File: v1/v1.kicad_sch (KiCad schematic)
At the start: 61 parts, among them CON1 SNES-CONN

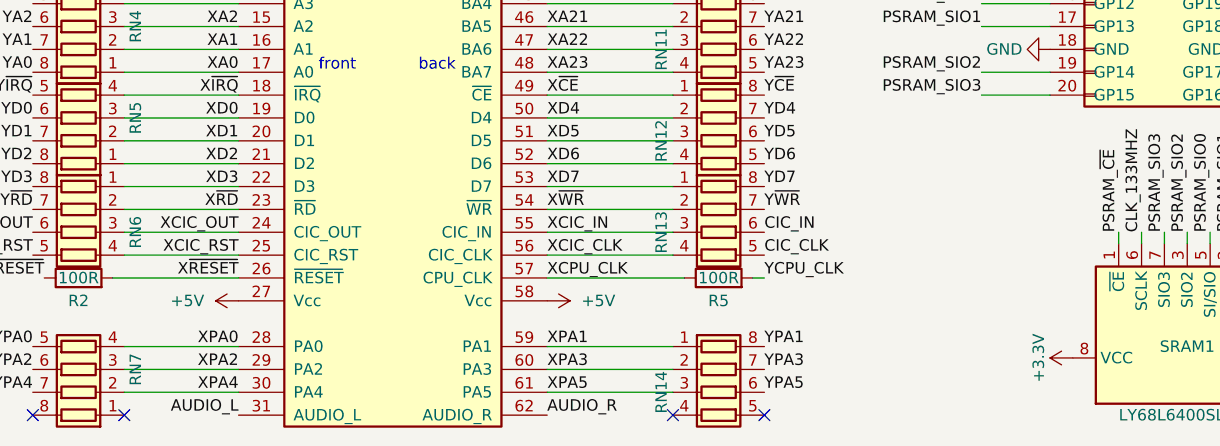
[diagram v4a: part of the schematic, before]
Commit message: v1: added jumper and diode for SNES 5V supply feeding +5V rail
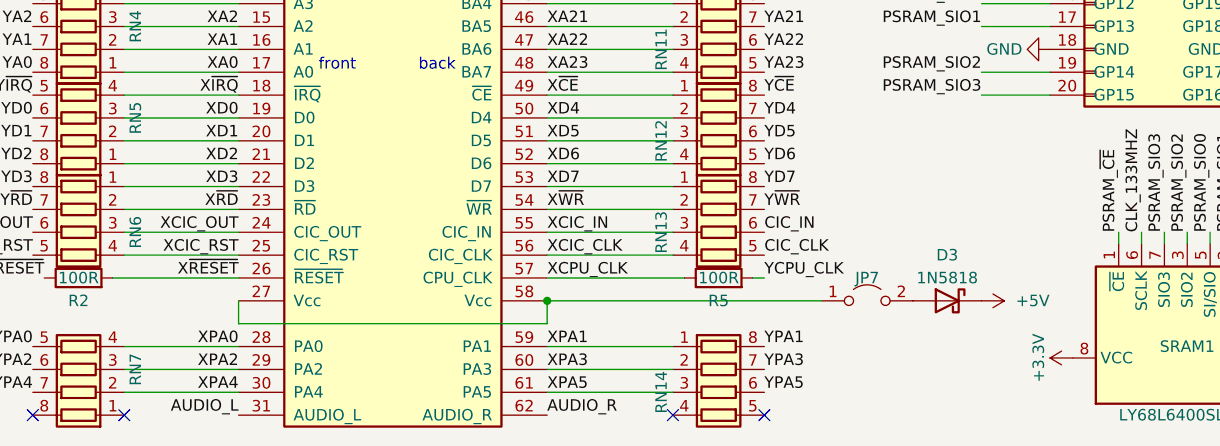
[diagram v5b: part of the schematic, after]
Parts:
- added D3: 1N5818, Diode_THT:D_DO-41_SOD81_P7.62mm_Horizontal, symbol Diode:1N5818
- added JP7: SNES_5V_OUT, Connector_PinHeader_2.54mm:PinHeader_1x02_P2.54mm_Vertical, symbol Jumper:Jumper_2_Open
- JP2: value PICO_3V3_EN -> PICO_3V3_OUT
- JP3: value CLK_OR_WRAM -> WRAM_OR_CLK
- JP4: value SNES_3V3_EN -> LDO_3V3_OUT
- JP5: value LDO_EN -> LDO_5V_IN
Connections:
- net +5V: now also D3.1 (K); no longer CON1.27 (Vcc), CON1.58 (Vcc)
- new net: CON1.27 (Vcc), CON1.58 (Vcc), JP7.1 (A)
- new net: D3.2 (A), JP7.2 (B)
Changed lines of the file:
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@@
   (junction (at 240.03 96.52) (diameter 0) (color 0 0 0 0)
   )
+  (junction (at 86.36 182.88) (diameter 0) (color 0 0 0 0)
+  )
   (junction (at 114.3 19.05) (diameter 0) (color 0 0 0 0)
   )
@@
     (stroke (width 0) (type default) (color 0 0 0 0))
   )
+  (wire (pts (xy 52.07 185.42) (xy 86.36 185.42))
+    (stroke (width 0) (type default) (color 0 0 0 0))
+  )
   (wire (pts (xy 264.16 121.92) (xy 274.32 121.92))
     (stroke (width 0) (type default) (color 0 0 0 0))
@@
     (stroke (width 0) (type default) (color 0 0 0 0))
   )
+  (wire (pts (xy 116.84 182.88) (xy 86.36 182.88))
+    (stroke (width 0) (type default) (color 0 0 0 0))
+  )
   (wire (pts (xy 134.62 132.08) (xy 142.24 132.08))
     (stroke (width 0) (type default) (color 0 0 0 0))
@@
     (stroke (width 0) (type default) (color 0 0 0 0))
   )
+  (wire (pts (xy 52.07 182.88) (xy 52.07 185.42))
+    (stroke (width 0) (type default) (color 0 0 0 0))
+  )
   (wire (pts (xy 100.33 167.64) (xy 86.36 167.64))
     (stroke (width 0) (type default) (color 0 0 0 0))
@@
     (stroke (width 0) (type default) (color 0 0 0 0))
   )
+  (wire (pts (xy 86.36 182.88) (xy 86.36 185.42))
+    (stroke (width 0) (type default) (color 0 0 0 0))
+  )
   (wire (pts (xy 274.32 25.4) (xy 274.32 29.21))
     (stroke (width 0) (type default) (color 0 0 0 0))
@@
     (in_bom yes) (on_board yes)
     (property "Reference" "JP4" (id 0) (at 278.13 148.59 0))
-    (property "Value" "SNES_3V3_EN" (id 1) (at 276.86 148.59 0)
+    (property "Value" "LDO_3V3_OUT" (id 1) (at 276.86 148.59 0)
       (effects (font (size 1.27 1.27)) hide)
     )
@@
     (pin "1")
   )
-  (symbol (lib_id "power:+5V") (at 52.07 182.88 90) (unit 1)
-    (in_bom yes) (on_board yes) (fields_autoplaced)
-    (property "Reference" "#PWR07" (id 0) (at 55.88 182.88 0)
-      (effects (font (size 1.27 1.27)) hide)
-    )
-    (property "Value" "+5V" (id 1) (at 48.26 182.8799 90)
-      (effects (font (size 1.27 1.27)) (justify left))
-    )
-    (property "Footprint" "" (id 2) (at 52.07 182.88 0)
-      (effects (font (size 1.27 1.27)) hide)
-    )
-    (property "Datasheet" "" (id 3) (at 52.07 182.88 0)
-      (effects (font (size 1.27 1.27)) hide)
-    )
-    (pin "1")
-  )
   (symbol (lib_id "power:+3.3V") (at 186.69 69.85 0) (unit 1)
     (in_bom yes) (on_board yes)
@@
     (pin "2")
   )
-  (symbol (lib_id "power:+5V") (at 86.36 182.88 270) (unit 1)
-    (in_bom yes) (on_board yes) (fields_autoplaced)
-    (property "Reference" "#PWR014" (id 0) (at 82.55 182.88 0)
-      (effects (font (size 1.27 1.27)) hide)
-    )
-    (property "Value" "+5V" (id 1) (at 90.17 182.8799 90)
-      (effects (font (size 1.27 1.27)) (justify left))
-    )
-    (property "Footprint" "" (id 2) (at 86.36 182.88 0)
-      (effects (font (size 1.27 1.27)) hide)
-    )
-    (property "Datasheet" "" (id 3) (at 86.36 182.88 0)
-      (effects (font (size 1.27 1.27)) hide)
-    )
-    (pin "1")
-  )
   (symbol (lib_id "power:GND") (at 261.62 114.3 90) (unit 1)
     (in_bom yes) (on_board yes)
@@
     (pin "1")
   )
+  (symbol (lib_id "Jumper:Jumper_2_Open") (at 121.92 182.88 0) (unit 1)
+    (in_bom yes) (on_board yes)
+    (property "Reference" "JP7" (id 0) (at 121.92 180.34 0))
+    (property "Value" "SNES_5V_OUT" (id 1) (at 121.92 179.07 0)
+      (effects (font (size 1.27 1.27)) hide)
+    )
+    (property "Footprint" "Connector_PinHeader_2.54mm:PinHeader_1x02_P2.54mm_Vertical" (id 2) (at 121.92 182.88 0)
+      (effects (font (size 1.27 1.27)) hide)
+    )
+    (property "Datasheet" "~" (id 3) (at 121.92 182.88 0)
+      (effects (font (size 1.27 1.27)) hide)
+    )
+    (pin "1")
+    (pin "2")
+  )
   (symbol (lib_id "Device:R_Pack04") (at 34.29 175.26 90) (mirror x) (unit 1)
     (in_bom yes) (on_board yes)
@@
     (in_bom yes) (on_board yes)
     (property "Reference" "JP2" (id 0) (at 172.72 119.38 0))
-    (property "Value" "PICO_3V3_EN" (id 1) (at 172.72 118.11 0)
+    (property "Value" "PICO_3V3_OUT" (id 1) (at 172.72 118.11 0)
       (effects (font (size 1.27 1.27)) hide)
     )
@@
     (pin "2")
   )
+  (symbol (lib_id "Diode:1N5818") (at 130.81 182.88 0) (mirror y) (unit 1)
+    (in_bom yes) (on_board yes)
+    (property "Reference" "D3" (id 0) (at 130.81 177.8 0))
+    (property "Value" "1N5818" (id 1) (at 130.81 180.34 0))
+    (property "Footprint" "Diode_THT:D_DO-41_SOD81_P7.62mm_Horizontal" (id 2) (at 130.81 187.325 0)
+      (effects (font (size 1.27 1.27)) hide)
+    )
+    (property "Datasheet" "http://www.vishay.com/docs/88525/1n5817.pdf" (id 3) (at 130.81 182.88 0)
+      (effects (font (size 1.27 1.27)) hide)
+    )
+    (pin "1")
+    (pin "2")
+  )
   (symbol (lib_id "power:GND") (at 142.24 154.94 270) (mirror x) (unit 1)
     (in_bom yes) (on_board yes)
@@
     (pin "1")
   )
+  (symbol (lib_id "power:+5V") (at 134.62 182.88 270) (unit 1)
+    (in_bom yes) (on_board yes) (fields_autoplaced)
+    (property "Reference" "#PWR07" (id 0) (at 130.81 182.88 0)
+      (effects (font (size 1.27 1.27)) hide)
+    )
+    (property "Value" "+5V" (id 1) (at 138.43 182.8799 90)
+      (effects (font (size 1.27 1.27)) (justify left))
+    )
+    (property "Footprint" "" (id 2) (at 134.62 182.88 0)
+      (effects (font (size 1.27 1.27)) hide)
+    )
+    (property "Datasheet" "" (id 3) (at 134.62 182.88 0)
+      (effects (font (size 1.27 1.27)) hide)
+    )
+    (pin "1")
+  )
   (symbol (lib_id "Jumper:Jumper_2_Open") (at 171.45 111.76 0) (unit 1)
     (in_bom yes) (on_board yes)
@@
     (in_bom yes) (on_board yes)
     (property "Reference" "JP5" (id 0) (at 227.33 148.59 0))
-    (property "Value" "LDO_EN" (id 1) (at 226.06 148.59 0)
+    (property "Value" "LDO_5V_IN" (id 1) (at 226.06 148.59 0)
       (effects (font (size 1.27 1.27)) hide)
     )
@@
     (in_bom yes) (on_board yes)
     (property "Reference" "JP3" (id 0) (at 190.5 144.78 0))
-    (property "Value" "CLK_OR_WRAM" (id 1) (at 190.5 144.78 0)
+    (property "Value" "WRAM_OR_CLK" (id 1) (at 190.5 144.78 0)
       (effects (font (size 1.27 1.27)) hide)
     )
@@
       (reference "#PWR06") (unit 1) (value "GND") (footprint "")
     )
-    (path "/446b50e3-d5dd-4629-b069-e1a4e1595f4d"
+    (path "/a5ea402c-1803-4980-b84c-d40f3ad7494a"
       (reference "#PWR07") (unit 1) (value "+5V") (footprint "")
     )
@@
       (reference "#PWR013") (unit 1) (value "GND") (footprint "")
     )
-    (path "/474e97d0-0a22-4649-9c42-09e2d20e4807"
-      (reference "#PWR014") (unit 1) (value "+5V") (footprint "")
-    )
     (path "/09fd768c-0ef6-4c93-9204-7613795fa6e3"
       (reference "#PWR015") (unit 1) (value "+3.3V") (footprint "")
@@
       (reference "D2") (unit 1) (value "1N5818") (footprint "Diode_THT:D_DO-41_SOD81_P7.62mm_Horizontal")
     )
+    (path "/930b6c54-1e41-4b78-8840-ffa529cc51d7"
+      (reference "D3") (unit 1) (value "1N5818") (footprint "Diode_THT:D_DO-41_SOD81_P7.62mm_Horizontal")
+    )
     (path "/ca930da2-15aa-497f-bd76-01155c6da4f5"
       (reference "ICSP1") (unit 1) (value "PIC12_ICSP") (footprint "Connector_PinHeader_2.54mm:PinHeader_1x05_P2.54mm_Vertical")
@@
     )
     (path "/91f03a91-b485-4f6d-9ee4-5587c47c3b9b"
-      (reference "JP2") (unit 1) (value "PICO_3V3_EN") (footprint "Connector_PinHeader_2.54mm:PinHeader_1x02_P2.54mm_Vertical")
+      (reference "JP2") (unit 1) (value "PICO_3V3_OUT") (footprint "Connector_PinHeader_2.54mm:PinHeader_1x02_P2.54mm_Vertical")
     )
     (path "/ed452612-d54f-4b1a-ad2a-275d9b6b5051"
-      (reference "JP3") (unit 1) (value "CLK_OR_WRAM") (footprint "Connector_PinHeader_2.54mm:PinHeader_1x03_P2.54mm_Vertical")
+      (reference "JP3") (unit 1) (value "WRAM_OR_CLK") (footprint "Connector_PinHeader_2.54mm:PinHeader_1x03_P2.54mm_Vertical")
     )
     (path "/28fc5943-be68-4787-adda-0804e71a7ae7"
-      (reference "JP4") (unit 1) (value "SNES_3V3_EN") (footprint "Connector_PinHeader_2.54mm:PinHeader_1x02_P2.54mm_Vertical")
+      (reference "JP4") (unit 1) (value "LDO_3V3_OUT") (footprint "Connector_PinHeader_2.54mm:PinHeader_1x02_P2.54mm_Vertical")
     )
     (path "/e4fe0cc7-7111-42d8-8ea3-f52cec8eaf51"
-      (reference "JP5") (unit 1) (value "LDO_EN") (footprint "Connector_PinHeader_2.54mm:PinHeader_1x02_P2.54mm_Vertical")
+      (reference "JP5") (unit 1) (value "LDO_5V_IN") (footprint "Connector_PinHeader_2.54mm:PinHeader_1x02_P2.54mm_Vertical")
     )
     (path "/a85df663-43ef-445d-b571-fbcc7c3633b0"
       (reference "JP6") (unit 1) (value "PICO_5V_OUT") (footprint "Connector_PinHeader_2.54mm:PinHeader_1x02_P2.54mm_Vertical")
     )
+    (path "/747199cd-0a65-42c2-b2da-90c0b9989247"
+      (reference "JP7") (unit 1) (value "SNES_5V_OUT") (footprint "Connector_PinHeader_2.54mm:PinHeader_1x02_P2.54mm_Vertical")
+    )
     (path "/19a6613f-0c11-4974-96bc-f81c4928003e"

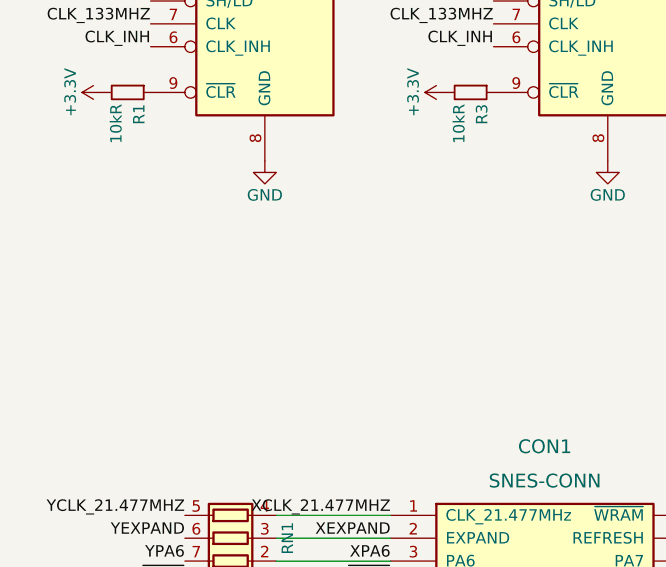
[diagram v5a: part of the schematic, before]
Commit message: v1: updated footprint of RPi Pico to include pin labels; added test points for power rails
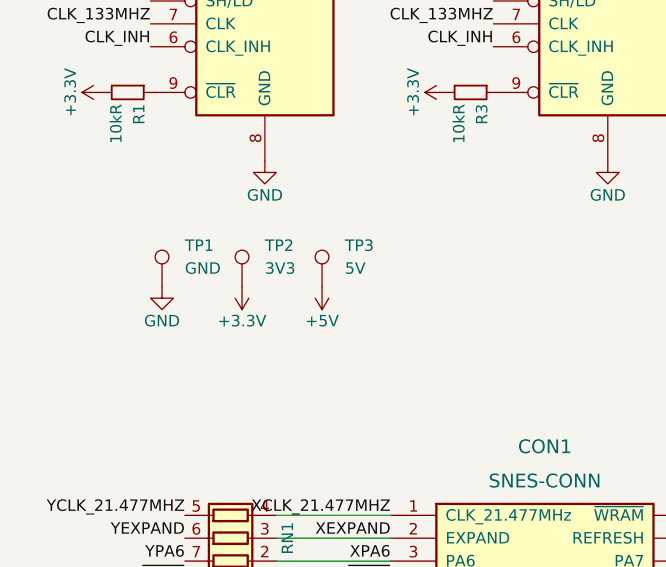
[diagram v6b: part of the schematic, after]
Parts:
- added TP1: GND, TestPoint:TestPoint_THTPad_D2.0mm_Drill1.0mm, symbol Connector:TestPoint
- added TP2: 3V3, TestPoint:TestPoint_THTPad_D2.0mm_Drill1.0mm, symbol Connector:TestPoint
- added TP3: 5V, TestPoint:TestPoint_THTPad_D2.0mm_Drill1.0mm, symbol Connector:TestPoint
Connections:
- net +3.3V: now also TP2.1
- net +5V: now also TP3.1
- net GND: now also TP1.1
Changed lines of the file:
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@@
+    (pin "1")
+  )
+  (symbol (lib_id "Connector:TestPoint") (at 35.56 88.9 0) (unit 1)
+    (in_bom yes) (on_board yes) (fields_autoplaced)
+    (property "Reference" "TP2" (id 0) (at 38.1 84.3279 0)
+      (effects (font (size 1.27 1.27)) (justify left))
+    )
+    (property "Value" "3V3" (id 1) (at 38.1 86.8679 0)
+      (effects (font (size 1.27 1.27)) (justify left))
+    )
+    (property "Footprint" "TestPoint:TestPoint_THTPad_D2.0mm_Drill1.0mm" (id 2) (at 40.64 88.9 0)
+      (effects (font (size 1.27 1.27)) hide)
+    )
+    (property "Datasheet" "~" (id 3) (at 40.64 88.9 0)
+      (effects (font (size 1.27 1.27)) hide)
+    )
     (pin "1")
   )
@@
     (pin "9")
   )
+  (symbol (lib_id "power:GND") (at 26.67 88.9 0) (unit 1)
+    (in_bom yes) (on_board yes)
+    (property "Reference" "#PWR014" (id 0) (at 26.67 95.25 0)
+      (effects (font (size 1.27 1.27)) hide)
+    )
+    (property "Value" "GND" (id 1) (at 26.67 92.71 0))
+    (property "Footprint" "" (id 2) (at 26.67 88.9 0)
+      (effects (font (size 1.27 1.27)) hide)
+    )
+    (property "Datasheet" "" (id 3) (at 26.67 88.9 0)
+      (effects (font (size 1.27 1.27)) hide)
+    )
+    (pin "1")
+  )
   (symbol (lib_id "Device:R_Pack04") (at 34.29 152.4 90) (unit 1)
     (in_bom yes) (on_board yes)
@@
     (pin "2")
   )
+  (symbol (lib_id "Connector:TestPoint") (at 44.45 88.9 0) (unit 1)
+    (in_bom yes) (on_board yes) (fields_autoplaced)
+    (property "Reference" "TP3" (id 0) (at 46.99 84.3279 0)
+      (effects (font (size 1.27 1.27)) (justify left))
+    )
+    (property "Value" "5V" (id 1) (at 46.99 86.8679 0)
+      (effects (font (size 1.27 1.27)) (justify left))
+    )
+    (property "Footprint" "TestPoint:TestPoint_THTPad_D2.0mm_Drill1.0mm" (id 2) (at 49.53 88.9 0)
+      (effects (font (size 1.27 1.27)) hide)
+    )
+    (property "Datasheet" "~" (id 3) (at 49.53 88.9 0)
+      (effects (font (size 1.27 1.27)) hide)
+    )
+    (pin "1")
+  )
   (symbol (lib_id "power:GND") (at 196.85 24.13 90) (unit 1)
     (in_bom yes) (on_board yes)
@@
     (pin "2")
   )
+  (symbol (lib_id "power:+3.3V") (at 35.56 88.9 0) (mirror x) (unit 1)
+    (in_bom yes) (on_board yes)
+    (property "Reference" "#PWR066" (id 0) (at 35.56 85.09 0)
+      (effects (font (size 1.27 1.27)) hide)
+    )
+    (property "Value" "+3.3V" (id 1) (at 35.56 92.71 0))
+    (property "Footprint" "" (id 2) (at 35.56 88.9 0)
+      (effects (font (size 1.27 1.27)) hide)
+    )
+    (property "Datasheet" "" (id 3) (at 35.56 88.9 0)
+      (effects (font (size 1.27 1.27)) hide)
+    )
+    (pin "1")
+  )
   (symbol (lib_id "Device:C_Small") (at 236.22 156.21 0) (mirror y) (unit 1)
     (in_bom yes) (on_board yes) (fields_autoplaced)
@@
     (pin "1")
     (pin "2")
+  )
+  (symbol (lib_id "Connector:TestPoint") (at 26.67 88.9 0) (unit 1)
+    (in_bom yes) (on_board yes) (fields_autoplaced)
+    (property "Reference" "TP1" (id 0) (at 29.21 84.3279 0)
+      (effects (font (size 1.27 1.27)) (justify left))
+    )
+    (property "Value" "GND" (id 1) (at 29.21 86.8679 0)
+      (effects (font (size 1.27 1.27)) (justify left))
+    )
+    (property "Footprint" "TestPoint:TestPoint_THTPad_D2.0mm_Drill1.0mm" (id 2) (at 31.75 88.9 0)
+      (effects (font (size 1.27 1.27)) hide)
+    )
+    (property "Datasheet" "~" (id 3) (at 31.75 88.9 0)
+      (effects (font (size 1.27 1.27)) hide)
+    )
+    (pin "1")
   )
   (symbol (lib_id "Device:R_Small") (at 60.96 67.31 270) (unit 1)
@@
     (pin "1")
   )
+  (symbol (lib_id "power:+5V") (at 44.45 88.9 180) (unit 1)
+    (in_bom yes) (on_board yes)
+    (property "Reference" "#PWR067" (id 0) (at 44.45 85.09 0)
+      (effects (font (size 1.27 1.27)) hide)
+    )
+    (property "Value" "+5V" (id 1) (at 44.45 92.71 0))
+    (property "Footprint" "" (id 2) (at 44.45 88.9 0)
+      (effects (font (size 1.27 1.27)) hide)
+    )
+    (property "Datasheet" "" (id 3) (at 44.45 88.9 0)
+      (effects (font (size 1.27 1.27)) hide)
+    )
+    (pin "1")
+  )
   (symbol (lib_id "Device:R_Pack04") (at 34.29 132.08 90) (unit 1)
     (in_bom yes) (on_board yes)
@@
       (reference "#PWR013") (unit 1) (value "GND") (footprint "")
     )
+    (path "/63de385d-203c-444a-b224-844cbe732cf7"
+      (reference "#PWR014") (unit 1) (value "GND") (footprint "")
+    )
     (path "/09fd768c-0ef6-4c93-9204-7613795fa6e3"
       (reference "#PWR015") (unit 1) (value "+3.3V") (footprint "")
@@
       (reference "#PWR065") (unit 1) (value "GND") (footprint "")
     )
+    (path "/a8ecaff4-ece3-4002-ad4b-d5c5486de256"
+      (reference "#PWR066") (unit 1) (value "+3.3V") (footprint "")
+    )
+    (path "/f6875e0f-5536-474e-8912-20f389b10b45"
+      (reference "#PWR067") (unit 1) (value "+5V") (footprint "")
+    )
     (path "/889aba05-c3aa-4aa2-95d3-b04e7b4f1745"
       (reference "#PWR0101") (unit 1) (value "GND") (footprint "")
@@
       (reference "SRAM1") (unit 1) (value "LY68L6400SLIT") (footprint "Package_SO:SOIC-8_3.9x4.9mm_P1.27mm")
     )
+    (path "/ac23a269-08f0-4220-845d-870fd0dde338"
+      (reference "TP1") (unit 1) (value "GND") (footprint "TestPoint:TestPoint_THTPad_D2.0mm_Drill1.0mm")
+    )
+    (path "/2bdb150d-a450-48b9-abdc-763b7011c6ce"
+      (reference "TP2") (unit 1) (value "3V3") (footprint "TestPoint:TestPoint_THTPad_D2.0mm_Drill1.0mm")
+    )
+    (path "/a0ccab81-cd0c-42c7-8472-0efffc489b82"
+      (reference "TP3") (unit 1) (value "5V") (footprint "TestPoint:TestPoint_THTPad_D2.0mm_Drill1.0mm")
+    )
     (path "/6cb4d886-2809-43f3-8700-1c11e70433f5"

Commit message: v1: added LCSC part numbers; switched out diodes for SMT; 74LV166A is out of stock at LCSC so need to replace it
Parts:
- ADDR1, ADDR2, ADDR3, ADDR4: LCSC (none) -> C2860649
- CON1: now left out of the parts list
- D1, D2, D3: footprint Diode_THT:D_DO-41_SOD81_P7.62mm_Horizontal -> Diode_SMD:D_SMA_Handsoldering; JLC (none) -> SMA; LCSC (none) -> C513476
- ICSP1: JLC SIP-5_2.5x12.7x2.54P -> Through hole straight pin header, 1x05, 2.54mm pitch, singl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; LCSC C492404 -> C390683
- JP1, JP2, JP4, JP5, JP6, JP7: JLC (none) -> Through hole straight pin header, 1x02, 2.54mm pitch, singl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; LCSC (none) -> C390678
- JP3: JLC (none) -> Through hole straight pin header, 1x03, 2.54mm pitch, singl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; LCSC (none) -> C390679
- LDO1: JLC SOT-223 -> SOT-223-3
- Pico1: LCSC (none) -> C429964
- R1, R2, R3, R4, R5, R6, R7, R8: JLC 1206_R -> 1206
- TXS1: JLC (none) -> SOT-23-6; LCSC (none) -> C2677420
